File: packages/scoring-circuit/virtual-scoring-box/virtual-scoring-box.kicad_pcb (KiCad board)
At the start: 4 copper layers, 120 x 85 mm, 122 parts, among them J1 GCT USB4105-GF-A, J2 STM SWD 3.3V, J3 LEFT WEAPON A B C, J4 RIGHT WEAPON A B C, J5 PISTE - NOT protective earth, J6 ESP 3.3V UART recovery, SW1 STM RESET, SW2 ESP RESET, SW3 ESP BOOT, T1 750315371, U1 STM32G474RET6, U10 SN74AXC1T45DCKR, U11 SN74AXC1T45DCKR, U13 TSOP38438, U18 CP2102N-A02-GQFN20R, U19 ISO7021DR, U2 ESP32-S3-WROOM-1-N8R8, U20 TLV75533PDBVR, U21 SN6505BDBVR, U22 TPS62162DSGR, U3 TPD2E2U06DCKR, U8 74LVC125APW, U9 74LVC125APW, Y1 ABM3B-8.000MHZ-B2-T

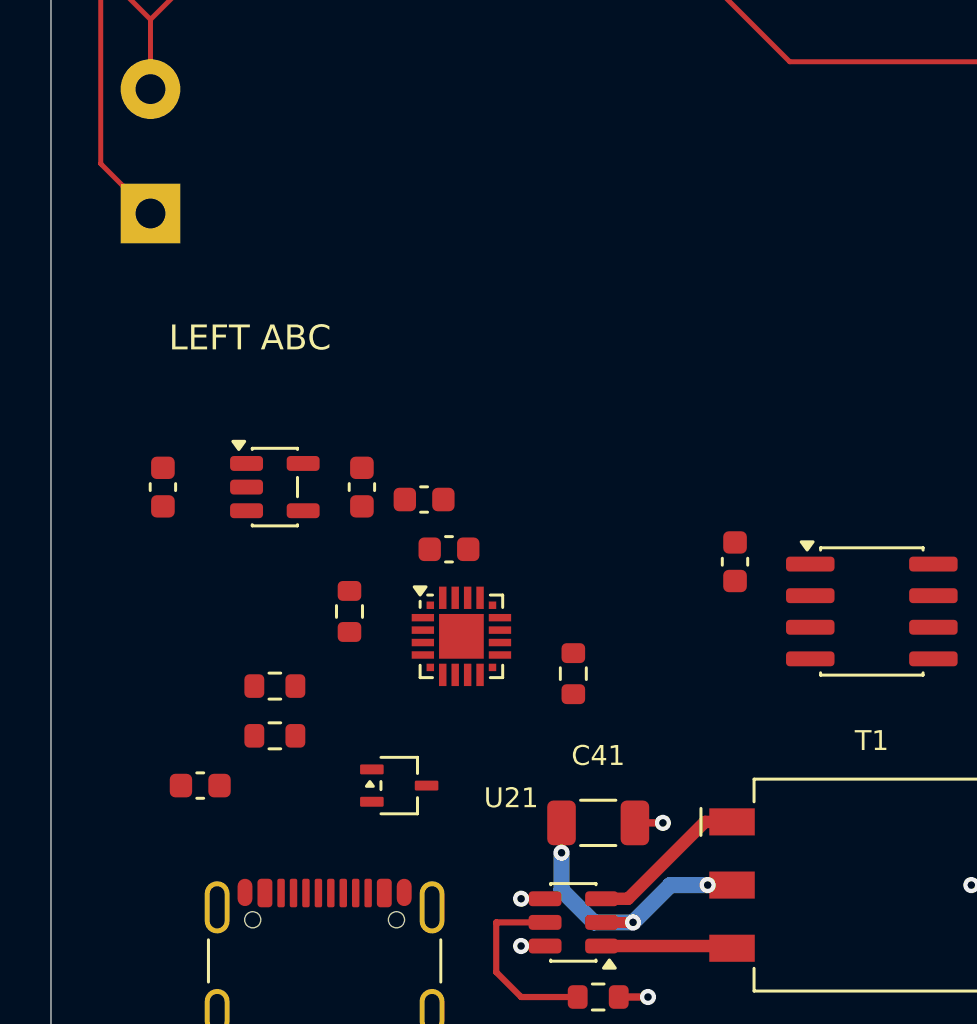
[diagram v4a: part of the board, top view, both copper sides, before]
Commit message: feat(scoring-circuit): integrate virtual-box USB-C source control
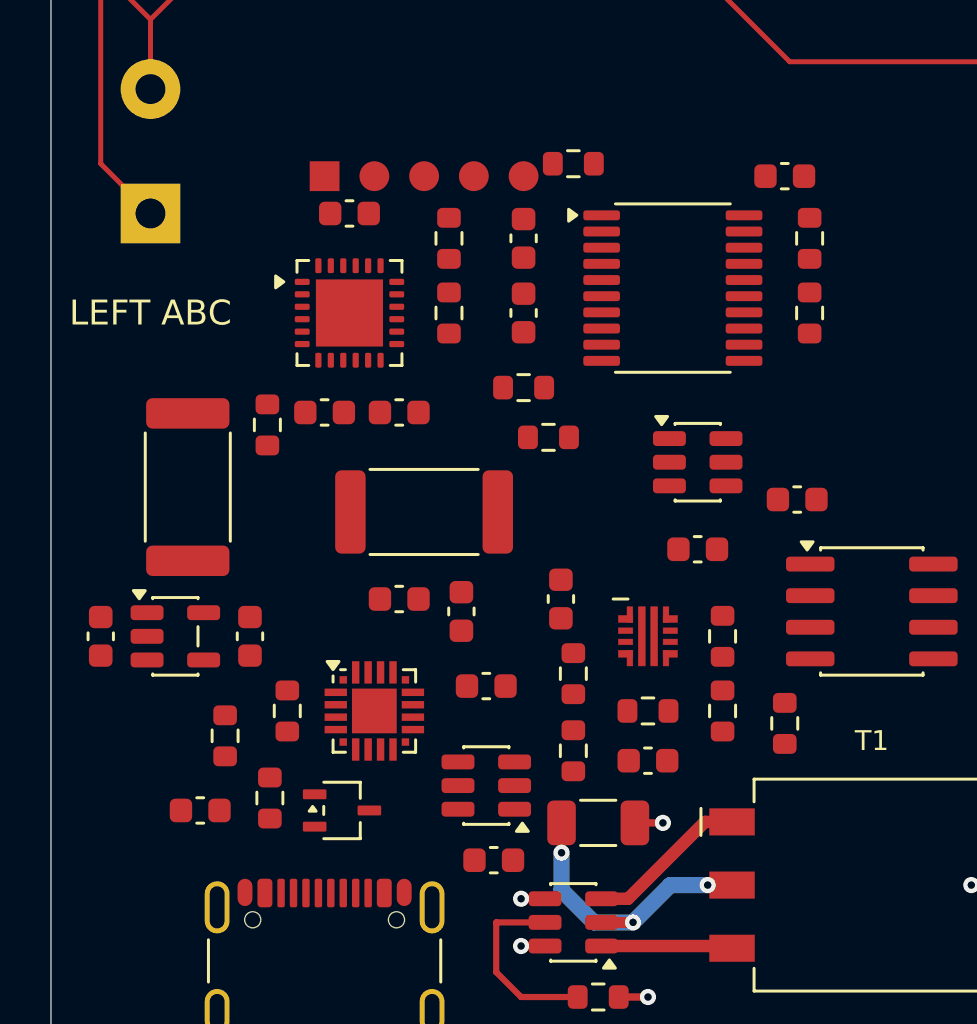
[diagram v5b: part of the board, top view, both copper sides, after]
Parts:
- added C48: 100nF, Capacitor_SMD:C_0603_1608Metric, F.Cu at (62.0, 100.0)
- added C49: 1uF, Capacitor_SMD:C_0603_1608Metric, F.Cu at (61.0, 108.0)
- added C50: 1uF, Capacitor_SMD:C_0603_1608Metric, F.Cu at (64.0, 108.0)
- added C51: 100nF, Capacitor_SMD:C_0603_1608Metric, F.Cu at (69.0, 101.0)
- added C52: 1uF, Capacitor_SMD:C_0603_1608Metric, F.Cu at (69.0, 104.0)
- added C53: 100nF, Capacitor_SMD:C_0603_1608Metric, F.Cu at (70.5, 115.5)
- added C54: 10nF, Capacitor_SMD:C_0603_1608Metric, F.Cu at (74.0, 122.0)
- added C55: 100nF, Capacitor_SMD:C_0603_1608Metric, F.Cu at (76.0, 113.5)
- added C56: 100nF, Capacitor_SMD:C_0603_1608Metric, F.Cu at (67.5, 119.0)
- added C57: 100nF, Capacitor_SMD:C_0603_1608Metric, F.Cu at (67.8, 126.0)
- added C58: 100nF, Capacitor_SMD:C_0603_1608Metric, F.Cu at (79.5, 98.5)
- added J7: PRIMARY SWD PADS, ScoringPlatform:Primary_SWD_Pads, F.Cu at (61.0, 98.5)
- added R81: 23.7k 0.1%, Resistor_SMD:R_0603_1608Metric, F.Cu at (71.0, 118.5)
- added R82: 10k 0.1%, Resistor_SMD:R_0603_1608Metric, F.Cu at (71.0, 121.6)
- added R83: 34.8k 0.1%, Resistor_SMD:R_0603_1608Metric, F.Cu at (77.0, 117.0)
- added R84: 10k 0.1%, Resistor_SMD:R_0603_1608Metric, F.Cu at (77.0, 120.0)
- added R85: 2.74k, Resistor_SMD:R_0603_1608Metric, F.Cu at (74.0, 120.0)
- added R86: 4.7k, Resistor_SMD:R_0603_1608Metric, F.Cu at (66.0, 101.0)
- added R87: 4.7k, Resistor_SMD:R_0603_1608Metric, F.Cu at (66.0, 104.0)
- added R88: 47k, Resistor_SMD:R_0603_1608Metric, F.Cu at (69.0, 107.0)
- added R89: 100k, Resistor_SMD:R_0603_1608Metric, F.Cu at (58.7, 108.5)
- added R90: 100k, Resistor_SMD:R_0603_1608Metric, F.Cu at (80.5, 101.0)
- added R91: 100k, Resistor_SMD:R_0603_1608Metric, F.Cu at (80.5, 104.0)
- added R92: 47k, Resistor_SMD:R_0603_1608Metric, F.Cu at (79.5, 120.5)
- added R93: 1k 1W, Resistor_SMD:R_2512_6332Metric, F.Cu at (55.5, 111.0)
- added R94: 1k 1W, Resistor_SMD:R_2512_6332Metric, F.Cu at (65.0, 112.0)
- added R95: 10k, Resistor_SMD:R_0603_1608Metric, F.Cu at (71.0, 98.0)
- added U23: STUSB4500QTR, ScoringPlatform:STUSB4500QTR, F.Cu at (62.0, 104.0)
- added U24: STM32C011F6P6, Package_SO:TSSOP-20_4.4x6.5mm_P0.65mm, F.Cu at (75.0, 103.0)
- added U25: TPS259470ARPWR, ScoringPlatform:TPS25947_RPW, F.Cu at (74.0, 117.0)
- added U26: SN74LVC1G3208DBVR, Package_TO_SOT_SMD:SOT-23-6, F.Cu at (76.0, 110.0)
- added U27: SN74LVC1T45DBVR, Package_TO_SOT_SMD:SOT-23-6, F.Cu at (67.5, 123.0)
- C40: value 1uF -> 4.7uF
- U20: value TLV75533PDBVR -> TPS70933DBVR
- moved R75 9.55 mm to (70.0, 109.0), turned to 0 degrees
- moved C40 7.50 mm to (58.0, 117.0)
- moved U20 7.21 mm to (55.0, 117.0)
- moved C39 6.50 mm to (52.0, 117.0)
- moved R74 4.72 mm to (59.5, 120.0)
- moved U18 4.61 mm to (63.0, 120.0)
- moved C35 4.12 mm to (64.0, 115.5)
- moved C37 3.54 mm to (80.0, 111.5), turned to 0 degrees
- moved R76 2.83 mm to (57.0, 121.0), turned to 90 degrees
- moved C36 2.55 mm to (66.5, 116.0), turned to 90 degrees
- moved R77 2.51 mm to (58.8, 123.5), turned to 90 degrees
- moved U3 2.51 mm to (61.7, 124.0)
- moved C1 1.00 mm to (56.0, 124.0)
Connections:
- R76 pad 1: USB_VBUS -> USB_5V_PROTECTED
- U20 pad 3: USB_VBUS -> unconnected-(U20-EN-Pad3)

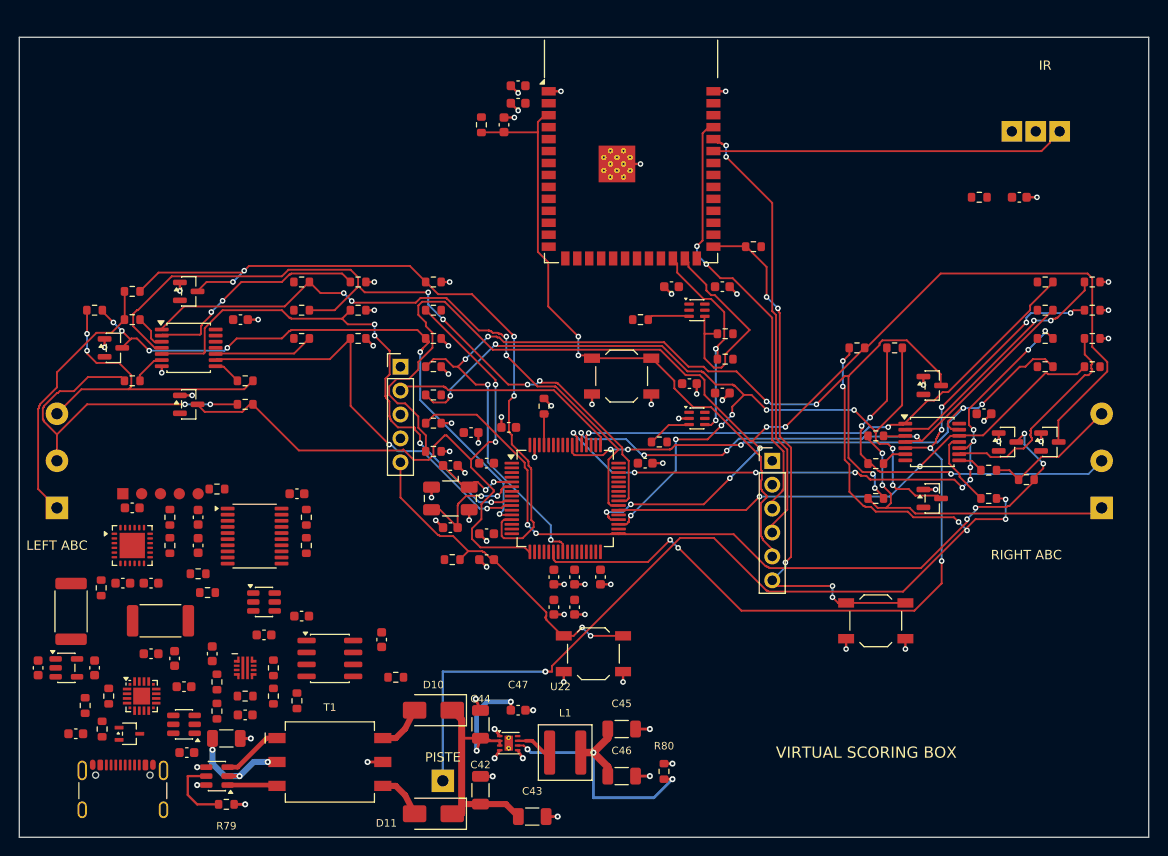
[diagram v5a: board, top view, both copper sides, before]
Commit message: feat(scoring-circuit): route virtual scoring box board
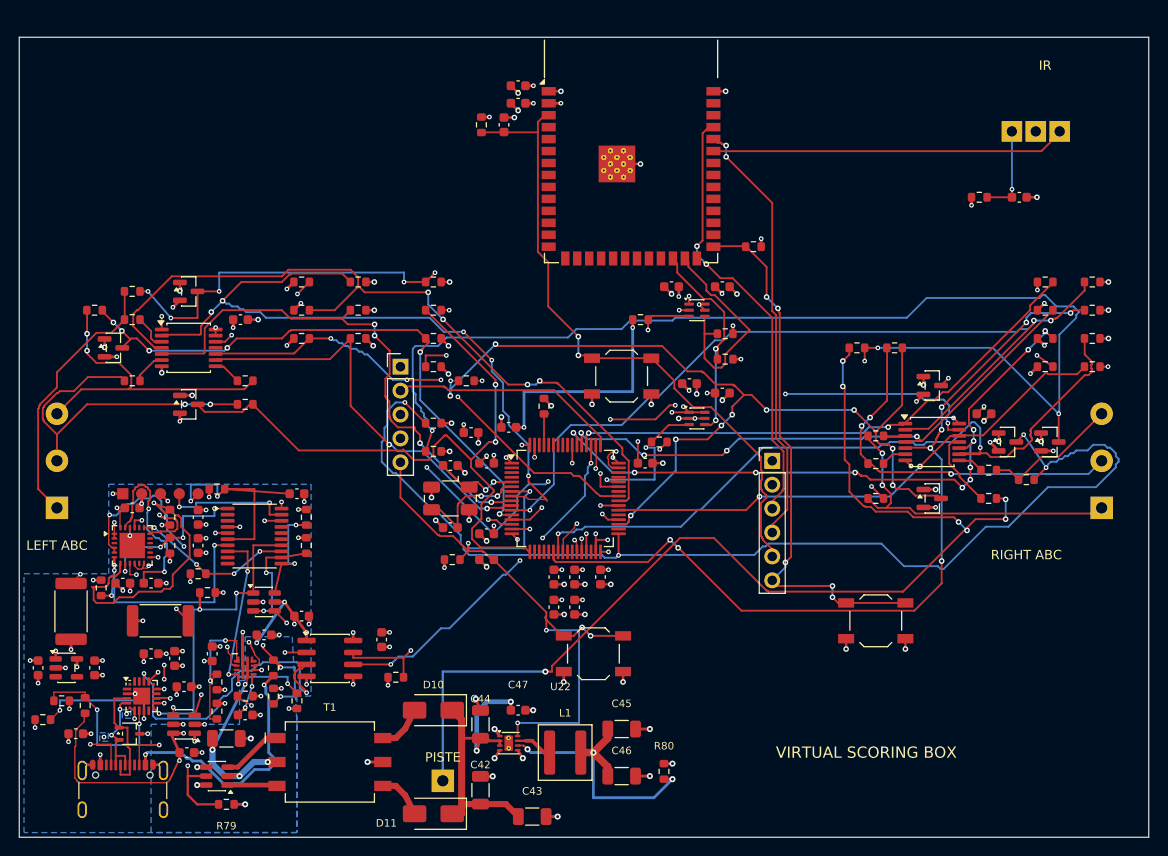
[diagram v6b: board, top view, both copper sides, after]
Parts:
- moved R74 7.43 mm to (52.5, 122.5), turned to 0 degrees
- moved R77 5.24 mm to (54.5, 120.5), turned to 0 degrees
- moved R69 3.81 mm to (97.5, 86.5)
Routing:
- net CORE_3V3: track 30.9 -> 112.2 mm, vias 3 -> 60
- net USB_VBUS: track 0.00 -> 74.3 mm, vias 0 -> 12
- net RIGHT_A_DRIVE: track 26.4 -> 93.1 mm, vias 2 -> 3
- net RIGHT_C_DRIVE: track 23.1 -> 80.2 mm, vias 0 -> 2
- net LEFT_A_DRIVE: track 24.0 -> 76.5 mm, vias 2 -> 5
- net PD_SCL: track 0.00 -> 46.6 mm, vias 0 -> 2
- net USB_CC2: track 0.00 -> 43.9 mm, vias 0 -> 5
- net LEFT_C_OE_N: track 10.7 -> 50.6 mm, vias 0 -> 4
- net STM_RESET_N: track 36.2 -> 74.2 mm, vias 2 -> 6
- net USB_CC1: track 0.00 -> 37.9 mm, vias 0 -> 2
- net LAPTOP_UART_RX: track 0.00 -> 37.7 mm, vias 0 -> 4
- net USB_HOST_3V3: track 0.00 -> 37.7 mm, vias 0 -> 23
- net USB_GND: track 4.22 -> 41.2 mm, vias 4 -> 46
- net USB_AWAKE: track 0.00 -> 35.3 mm, vias 0 -> 3
- net USB_5V_PROTECTED: track 12.0 -> 46.2 mm, vias 3 -> 6
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- added copper zone on In2.Cu, net CORE_3V3
- added copper zone on B.Cu, net USB_5V_PROTECTED
- added copper zone on B.Cu, net USB_GND
- added copper zone on In1.Cu, net USB_GND
- added copper zone on In2.Cu, net USB_HOST_3V3
- added copper zone on B.Cu, net USB_VBUS
- removed copper zone on In2.Cu, net USB_GND

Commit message: feat(scoring-circuit): simplify virtual-box UART and export assembly handoff
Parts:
- removed C23, C24, C25, C26: 100nF 10V, Capacitor_SMD:C_0603_1608Metric
- removed R30, R31: 47k, Resistor_SMD:R_0603_1608Metric
- removed U10, U11: SN74AXC1T45DCKR, ScoringPlatform:SN74AXC1T45DCKR
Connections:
- R73 pad 2: ESP_TX -> STM_RX
- U2 pad 24: ESP_TX -> STM_RX
- U2 pad 25: ESP_RX -> STM_TX
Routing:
- net STM_TX: track 25.1 -> 49.5 mm
- net ESP_RX: track 24.1 -> 0.00 mm
- net STM_RX: track 16.4 -> 40.5 mm, vias 2 -> 4
- net ESP_TX: track 22.4 -> 0.00 mm, vias 2 -> 0
- net CORE_3V3: track 112.2 -> 100.2 mm, vias 60 -> 50
- net GND: track 94.6 -> 87.0 mm, vias 81 -> 74
